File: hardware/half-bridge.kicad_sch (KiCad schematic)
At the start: 24 parts, among them J301 Phase_OUT, Q301 IPT015N10N5, Q302 IPT015N10N5, U301 IRS21867S, U302 INA240A2D

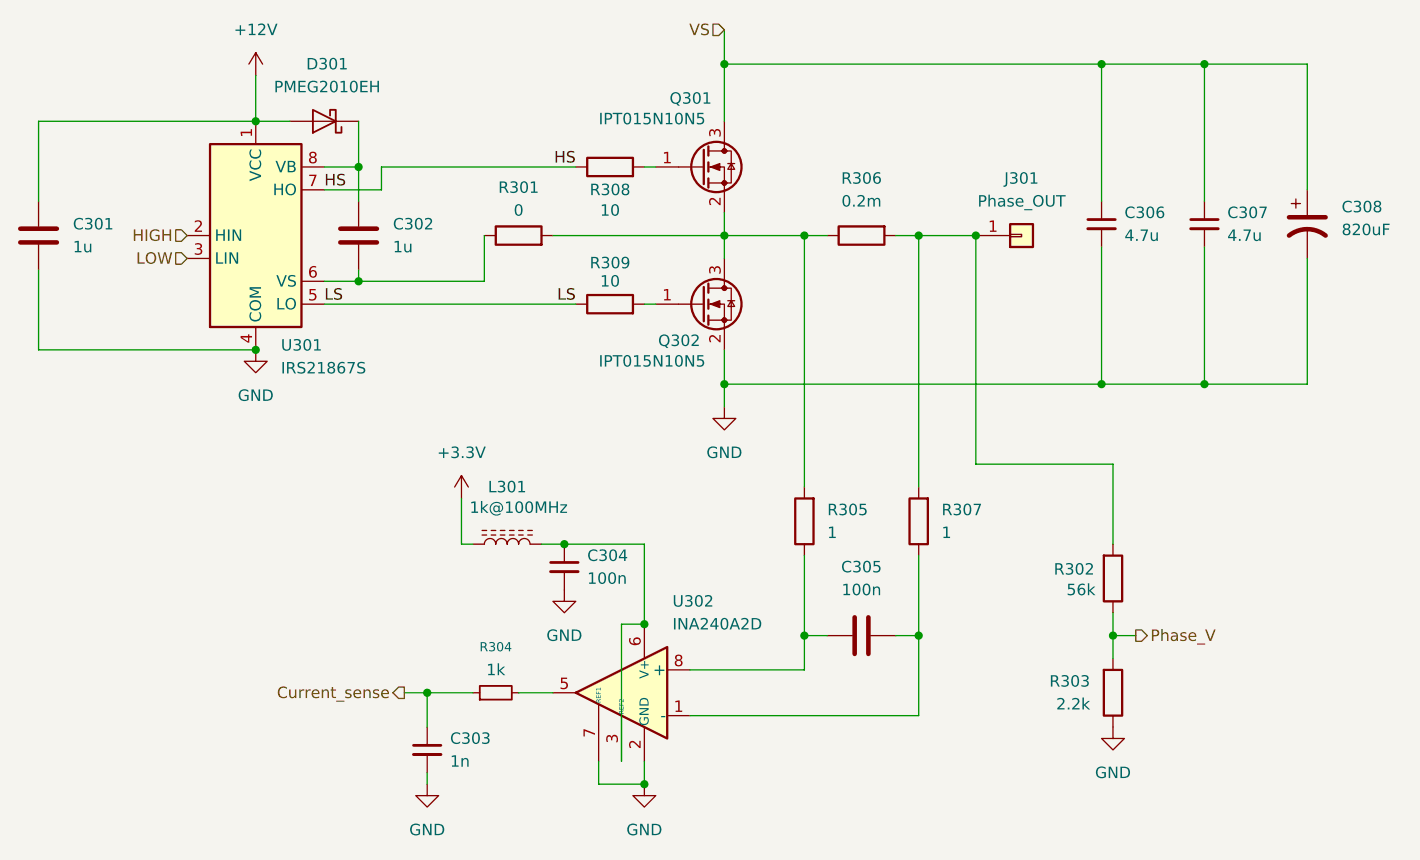
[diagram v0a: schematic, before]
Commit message: Reduce board size
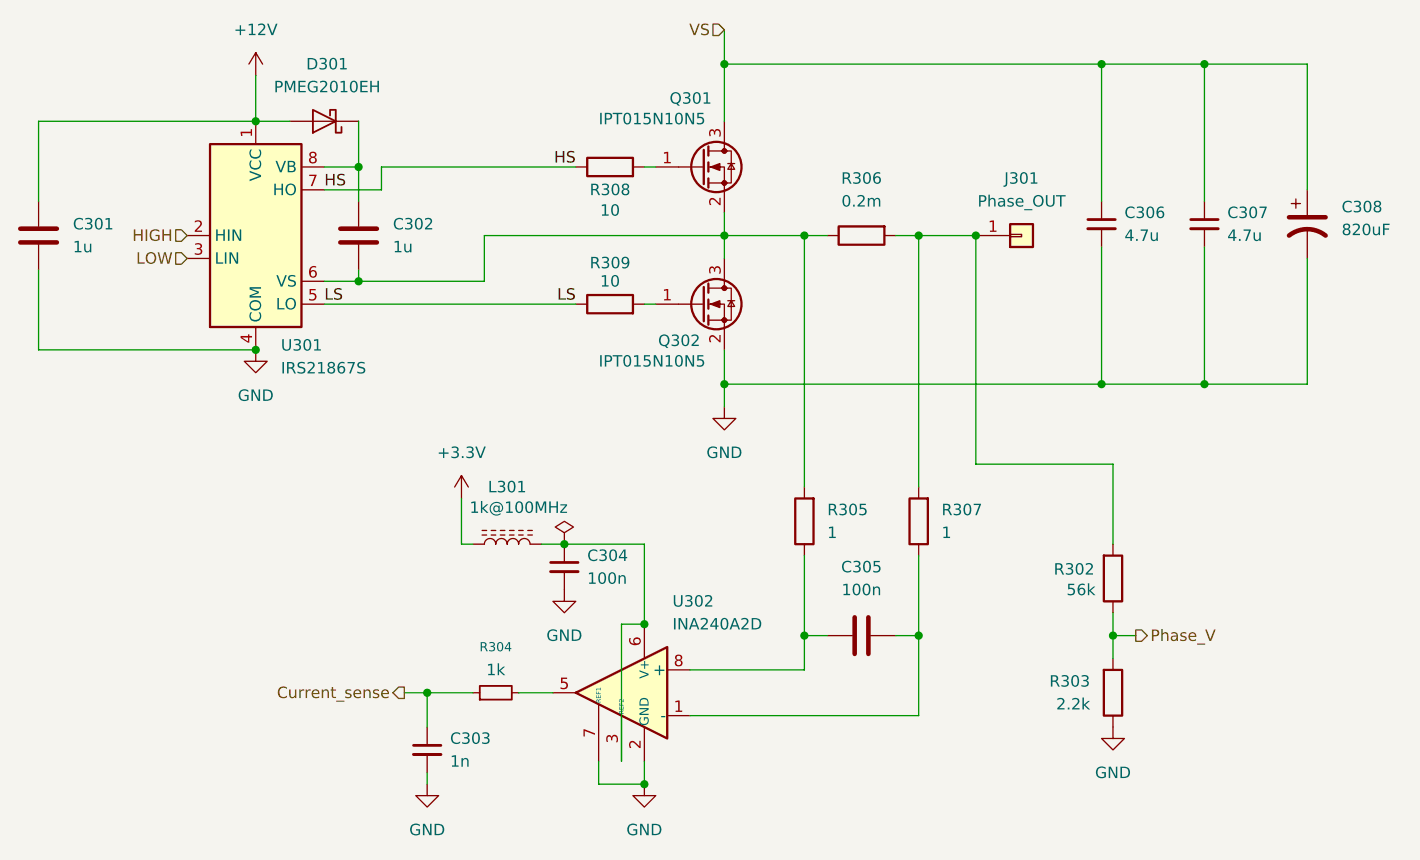
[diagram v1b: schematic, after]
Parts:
- removed R301: 0, Resistor_SMD:R_0805_2012Metric, symbol Device:R
- J301: footprint Connector_Wire:SolderWirePad_1x01_SMD_4x8mm -> MountingHole:MountingHole_3.2mm_M3_ISO14580_Pad_TopBottom
- R308, R309: footprint Resistor_SMD:R_0805_2012Metric -> Resistor_SMD:R_0603_1608Metric
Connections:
- net at Q301.2 (S), Q302.3 (D), R305.2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: now also C302.2, U301.6 (VS)
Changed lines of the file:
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@@
+	(wire
+		(pts
+			(xy 120.65 78.74) (xy 147.32 78.74)
+		)
+		(stroke
+			(width 0)
+			(type default)
+		)
+	)
 	(wire
 		(pts
@@
 		(pts
 			(xy 212.09 59.69) (xy 200.66 59.69)
-		)
-		(stroke
-			(width 0)
-			(type default)
-		)
-	)
-	(wire
-		(pts
-			(xy 128.27 78.74) (xy 147.32 78.74)
 		)
 		(stroke
@@
 			)
 		)
-		(property "Footprint" "Connector_Wire:SolderWirePad_1x01_SMD_4x8mm"
+		(property "Footprint" "MountingHole:MountingHole_3.2mm_M3_ISO14580_Pad_TopBottom"
 			(at 180.34 78.74 0)
 			(effects
@@
 	)
 	(symbol
+		(lib_id "power:PWR_FLAG")
+		(at 129.54 113.03 0)
+		(unit 1)
+		(exclude_from_sim no)
+		(in_bom yes)
+		(on_board yes)
+		(dnp no)
+		(fields_autoplaced yes)
+		(property "Reference" "#FLG0301"
+			(at 129.54 111.125 0)
+			(effects
+				(font
+					(size 1.27 1.27)
+				)
+				(hide yes)
+			)
+		)
+		(property "Value" "PWR_FLAG"
+			(at 129.54 107.95 0)
+			(effects
+				(font
+					(size 1.27 1.27)
+				)
+				(hide yes)
+			)
+		)
+		(property "Footprint" ""
+			(at 129.54 113.03 0)
+			(effects
+				(font
+					(size 1.27 1.27)
+				)
+				(hide yes)
+			)
+		)
+		(property "Datasheet" "~"
+			(at 129.54 113.03 0)
+			(effects
+				(font
+					(size 1.27 1.27)
+				)
+				(hide yes)
+			)
+		)
+		(property "Description" "Special symbol for telling ERC where power comes from"
+			(at 129.54 113.03 0)
+			(effects
+				(font
+					(size 1.27 1.27)
+				)
+				(hide yes)
+			)
+		)
+		(pin "1"
+		)
+		(instances
+			(project "greenmobi-drive"
+				(path "/a12b77e7-bd0f-4a70-9ba2-19a87ce48819/4a5d7eb9-ddee-45d4-92b5-174bd9809dbc"
+					(reference "#FLG0501")
+					(unit 1)
+				)
+				(path "/a12b77e7-bd0f-4a70-9ba2-19a87ce48819/caef660a-9a2f-49e8-a393-a85edb78ce64"
+					(reference "#FLG0401")
+					(unit 1)
+				)
+				(path "/a12b77e7-bd0f-4a70-9ba2-19a87ce48819/cd601179-baef-4e34-b5da-beea03762ae5"
+					(reference "#FLG0301")
+					(unit 1)
+				)
+			)
+		)
+	)
+	(symbol
 		(lib_id "Amplifier_Current:INA240A2D")
 		(at 135.89 129.54 0)
@@
 			)
 		)
-		(property "Footprint" "Resistor_SMD:R_0805_2012Metric"
+		(property "Footprint" "Resistor_SMD:R_0603_1608Metric"
 			(at 134.62 88.138 90)
 			(effects
@@
 	)
 	(symbol
-		(lib_id "Device:R")
-		(at 124.46 78.74 90)
-		(unit 1)
-		(exclude_from_sim no)
-		(in_bom yes)
-		(on_board yes)
-		(dnp no)
-		(property "Reference" "R301"
-			(at 124.46 73.406 90)
-			(effects
-				(font
-					(size 1.27 1.27)
-				)
-			)
-		)
-		(property "Value" "0"
-			(at 124.46 75.946 90)
-			(effects
-				(font
-					(size 1.27 1.27)
-				)
-			)
-		)
-		(property "Footprint" "Resistor_SMD:R_0805_2012Metric"
-			(at 124.46 80.518 90)
-			(effects
-				(font
-					(size 1.27 1.27)
-				)
-				(hide yes)
-			)
-		)
-		(property "Datasheet" "~"
-			(at 124.46 78.74 0)
-			(effects
-				(font
-					(size 1.27 1.27)
-				)
-				(hide yes)
-			)
-		)
-		(property "Description" "Resistor"
-			(at 124.46 78.74 0)
-			(effects
-				(font
-					(size 1.27 1.27)
-				)
-				(hide yes)
-			)
-		)
-		(property "LCSC" "C137513"
-			(at 124.46 78.74 90)
-			(effects
-				(font
-					(size 1.27 1.27)
-				)
-				(hide yes)
-			)
-		)
-		(pin "1"
-		)
-		(pin "2"
-		)
-		(instances
-			(project "greenmobi-drive"
-				(path "/a12b77e7-bd0f-4a70-9ba2-19a87ce48819/4a5d7eb9-ddee-45d4-92b5-174bd9809dbc"
-					(reference "R501")
-					(unit 1)
-				)
-				(path "/a12b77e7-bd0f-4a70-9ba2-19a87ce48819/caef660a-9a2f-49e8-a393-a85edb78ce64"
-					(reference "R401")
-					(unit 1)
-				)
-				(path "/a12b77e7-bd0f-4a70-9ba2-19a87ce48819/cd601179-baef-4e34-b5da-beea03762ae5"
-					(reference "R301")
-					(unit 1)
-				)
-			)
-		)
-	)
-	(symbol
 		(lib_id "power:+3.3V")
 		(at 118.11 107.95 0)
@@
 			)
 		)
-		(property "Footprint" "Resistor_SMD:R_0805_2012Metric"
+		(property "Footprint" "Resistor_SMD:R_0603_1608Metric"
 			(at 134.62 72.898 90)
 			(effects

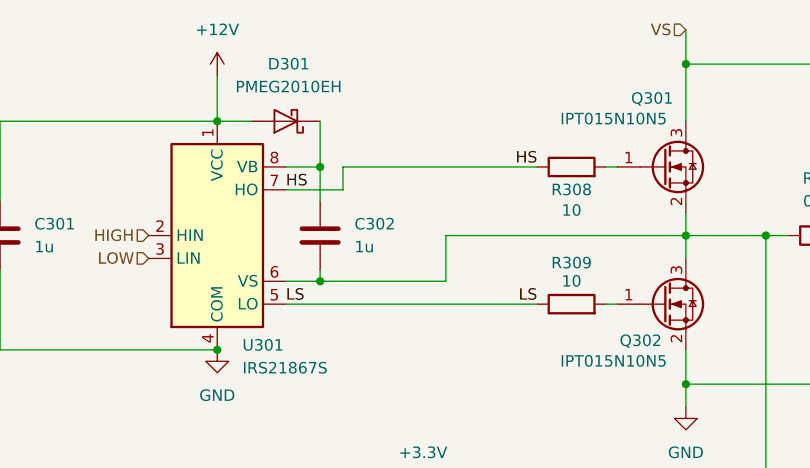
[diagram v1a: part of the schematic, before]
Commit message: Changed bootstrap diode and gate resistor
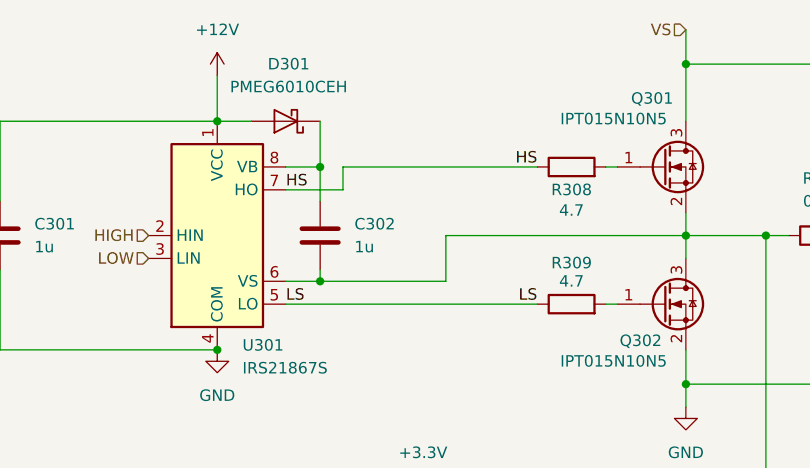
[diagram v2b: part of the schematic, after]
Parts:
- D301: value PMEG2010EH -> PMEG6010CEH; symbol Diode:PMEG2010EH -> Diode:PMEG6010CEH; LCSC C552825 -> C110797
- J301: footprint MountingHole:MountingHole_3.2mm_M3_ISO14580_Pad_TopBottom -> Connector_Wire:SolderWirePad_1x01_SMD_4x8mm
- R308, R309: value 10 -> 4.7; LCSC C17415 -> C25121
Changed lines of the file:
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@@
 			)
 		)
-		(property "Footprint" "MountingHole:MountingHole_3.2mm_M3_ISO14580_Pad_TopBottom"
+		(property "Footprint" "Connector_Wire:SolderWirePad_1x01_SMD_4x8mm"
 			(at 180.34 78.74 0)
 			(effects
@@
 			)
 		)
-		(property "Value" "10"
+		(property "Value" "4.7"
 			(at 134.62 83.82 90)
 			(effects
@@
 			)
 		)
-		(property "LCSC" "C17415"
+		(property "LCSC" "C25121"
 			(at 134.62 86.36 90)
 			(effects
@@
 	)
 	(symbol
-		(lib_id "Diode:PMEG2010EH")
+		(lib_id "Diode:PMEG6010CEH")
 		(at 102.87 66.04 180)
 		(unit 1)
@@
 			)
 		)
-		(property "Value" "PMEG2010EH"
+		(property "Value" "PMEG6010CEH"
 			(at 103.1875 62.23 0)
 			(effects
@@
 			)
 		)
-		(property "Datasheet" "https://assets.nexperia.com/documents/data-sheet/PMEG2010EH_EJ_ET.pdf"
+		(property "Datasheet" "https://assets.nexperia.com/documents/data-sheet/PMEG6010CEH_PMEG6010CEJ.pdf"
 			(at 102.87 66.04 0)
 			(effects
@@
 			)
 		)
-		(property "Description" "20V, 1A very low Vf MEGA Schottky barrier rectifier, SOD-123F"
+		(property "Description" "60V, 1A very low Vf MEGA Schottky barrier rectifier, SOD-123F"
 			(at 102.87 66.04 0)
 			(effects
@@
 			)
 		)
-		(property "LCSC" "C552825"
+		(property "LCSC" "C110797"
 			(at 102.87 66.04 0)
 			(effects
@@
 			)
 		)
-		(property "Value" "10"
+		(property "Value" "4.7"
 			(at 134.62 75.946 90)
 			(effects
@@
 			)
 		)
-		(property "LCSC" "C17415"
+		(property "LCSC" "C25121"
 			(at 134.62 71.12 90)
 			(effects
